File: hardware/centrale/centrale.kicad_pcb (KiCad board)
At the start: 2 copper layers, 70 x 110 mm, 57 parts, among them J1 MDCOG240128B6W, J2 Conn_BME280, J3 CONN_BME280_2, J4 RJ45, J5 Term_sel, Q1 BSS123, U1 MCP7940N-xSN, U2 TPS54228, U3 MCP2542FDxMF, Y1 32.768Khz

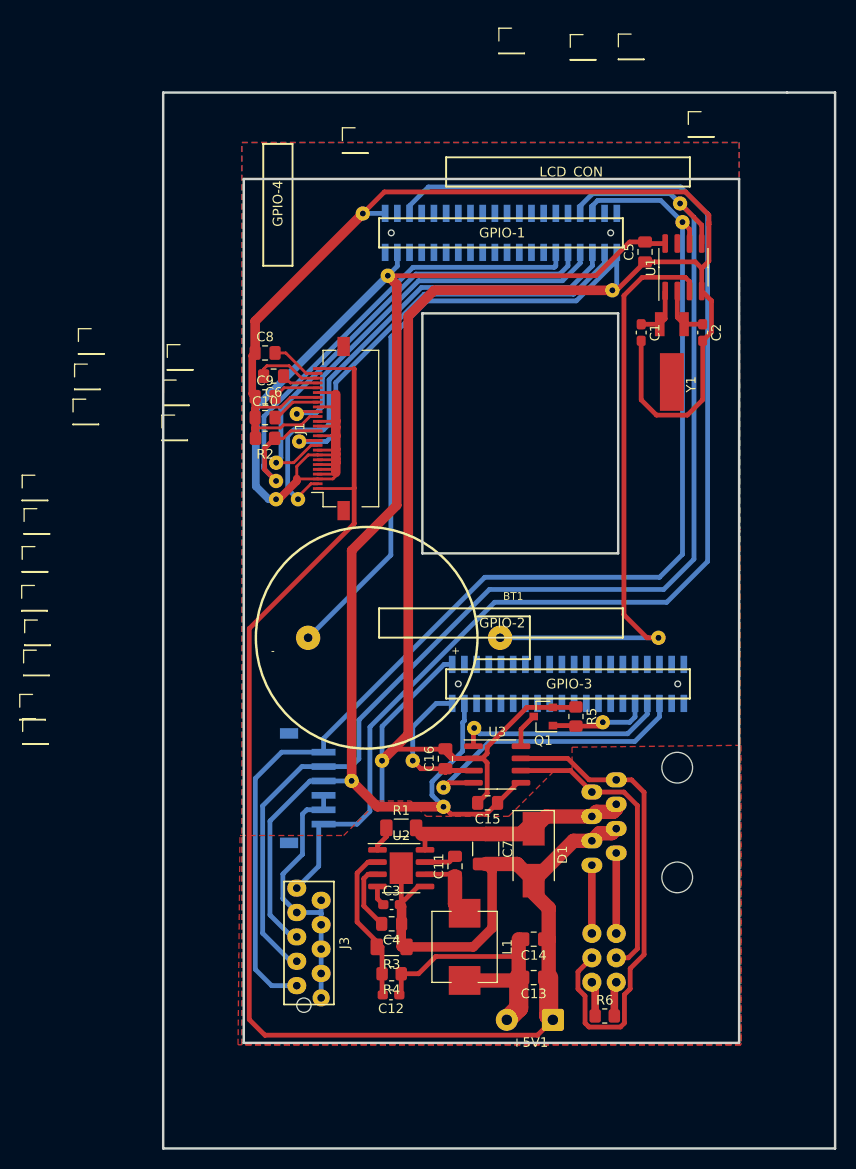
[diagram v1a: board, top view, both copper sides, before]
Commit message: Prepare for v2: fix display connector wiring, remplace the CAN transeiver with a pin-compatible one which is not out of stock, enlarge a bit the CPU cooling window.
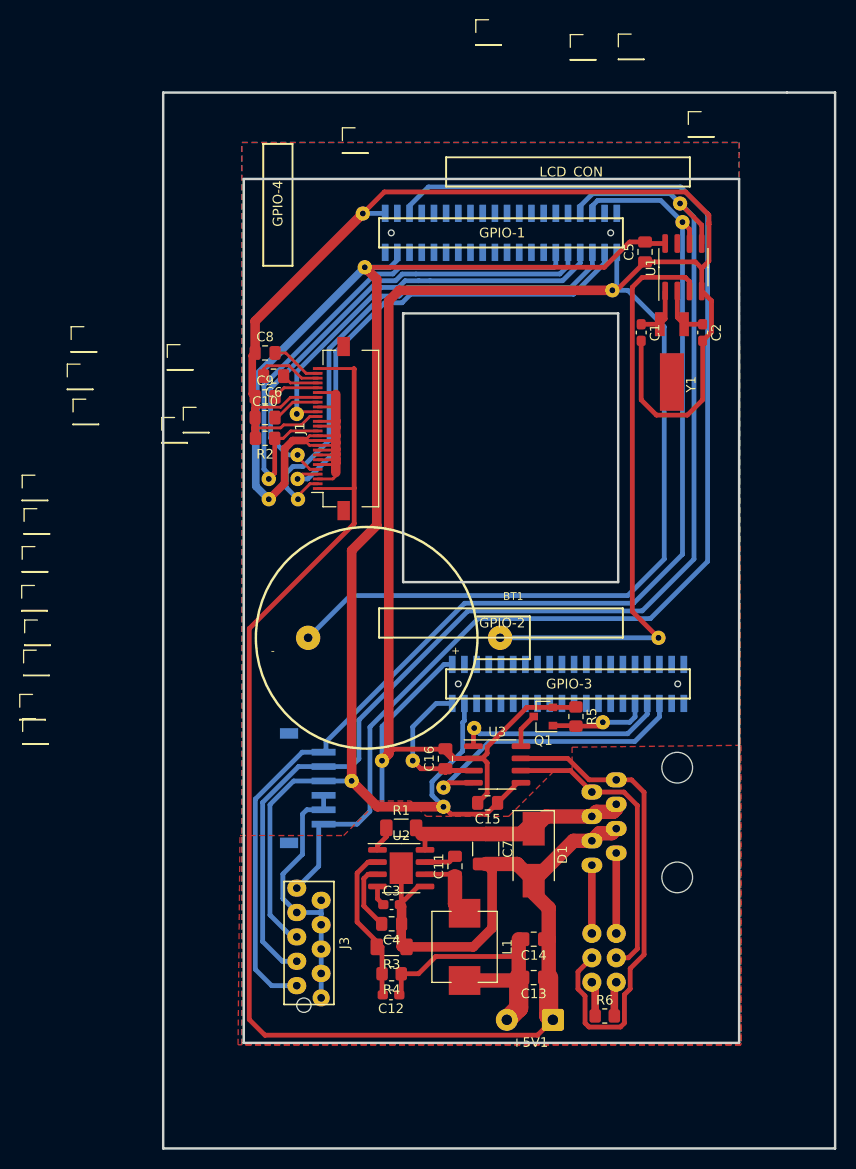
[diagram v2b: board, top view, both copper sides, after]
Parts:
- removed the REF** at (-42.5, -9.07)
- removed the REF** at (1.30, -40.4)
- added REF**: PinHeader_1x01_P2.54mm_Vertical, Connector_PinHeader_2.54mm:PinHeader_1x01_P2.54mm_Vertical, F.Cu at (-43.3, -9.28)
- added REF**: PinHeader_1x01_P2.54mm_Vertical, Connector_PinHeader_2.54mm:PinHeader_1x01_P2.54mm_Vertical, F.Cu at (-1.10, -41.3)
- U3: value MCP2542FDxMF -> TLE9250V
- moved REF** 3.90 mm to (-33.8, 0.18)
- moved REF** 2.37 mm to (-31.6, -0.88)
- moved REF** 0.76 mm to (-43.7, -5.38)
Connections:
- J1 pad 10: /D1-A0 -> +3V3
- J1 pad 11: /D0-SDA -> +3V3
- J1 pad 4: +3V3 -> /D0-SDA
- J1 pad 5: +3V3 -> /D1-A0
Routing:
- net GND: track 344.7 -> 355.9 mm
- net +3V3: track 216.1 -> 223.7 mm
- net /D0-SDA: track 45.6 -> 50.8 mm
- net /lime2/SCK: track 127.9 -> 126.3 mm
- net /V_BCKP: track 63.1 -> 61.7 mm
- net /SPI_CS: track 40.7 -> 42.0 mm
- net /SCL: track 52.9 -> 54.0 mm
- net /D1-A0: track 48.4 -> 49.2 mm
- net /lime2/SDA: track 130.9 -> 131.6 mm
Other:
- outline, holes or cut-outs redrawn

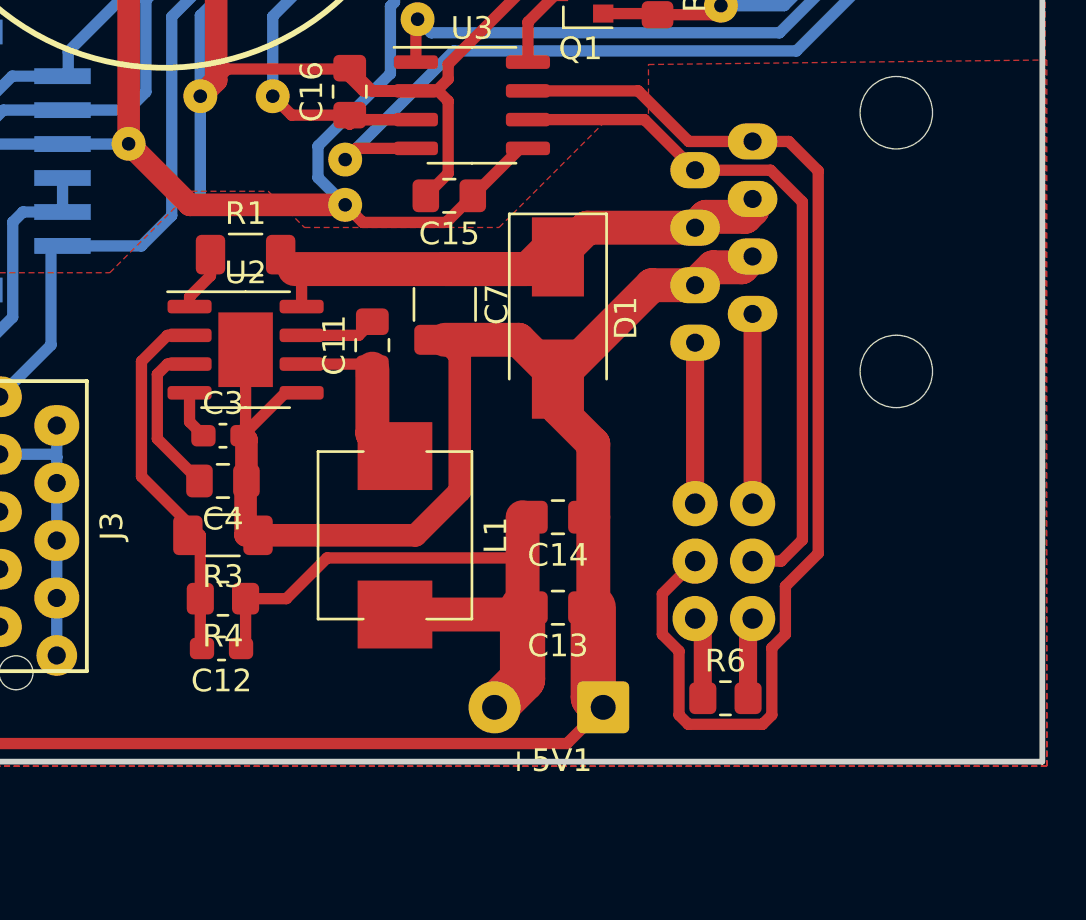
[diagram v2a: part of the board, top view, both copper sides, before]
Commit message: Use a MC24356 connector for the CPU power supply. Other minor cleanups
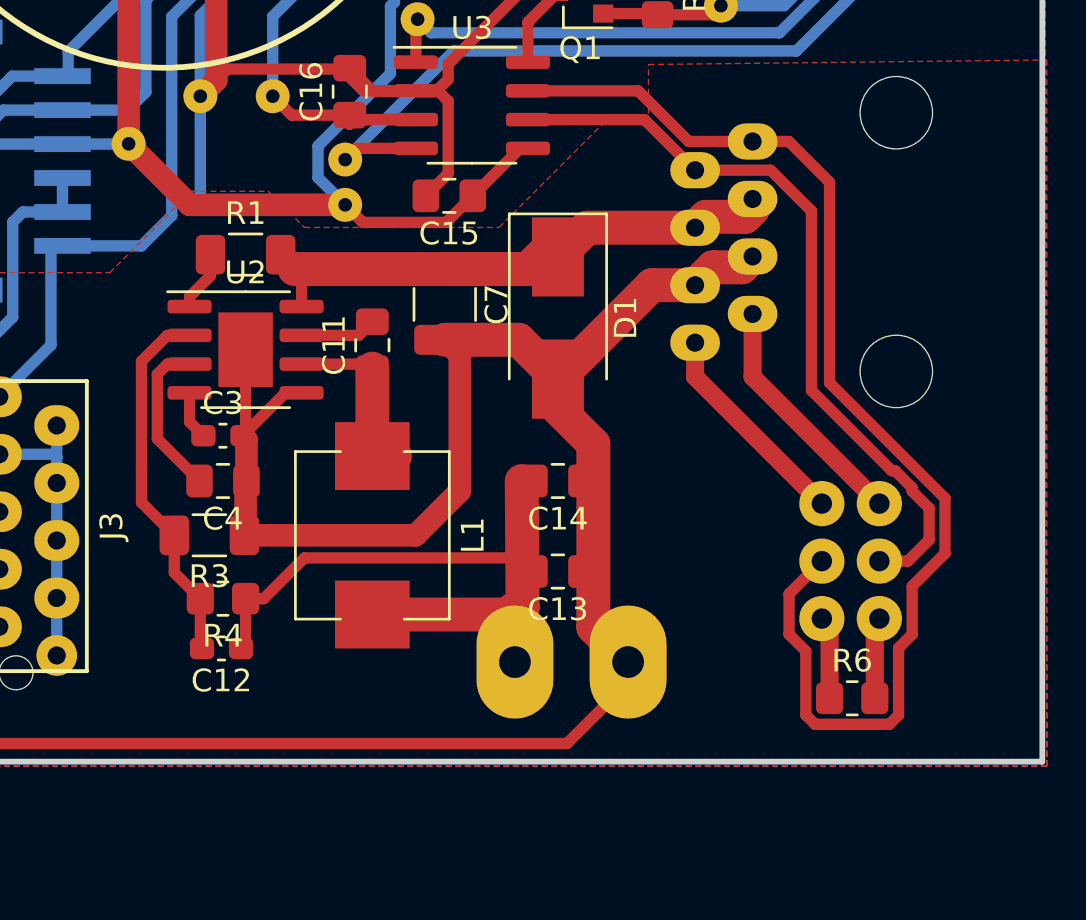
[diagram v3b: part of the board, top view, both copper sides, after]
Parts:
- +5V1: value CONN_01X02 -> 5V_LIME2; footprint Connector_Wire:SolderWire-0.5sqmm_1x02_P4.8mm_D0.9mm_OD2.3mm -> local:MC24356; moved to B.Cu
- moved J5 5.60 mm to (17.8, 52.6)
- moved R6 5.60 mm to (16.6, 61.2)
- moved +5V1 2.44 mm to (4.20, 59.6)
- moved C13 1.60 mm to (3.60, 55.6)
- moved C14 1.60 mm to (3.60, 51.6)
- moved L1 1.00 mm to (-4.60, 54.0)
- moved R3 0.60 mm to (-11.8, 54.0)
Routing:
- net Net-(J4-Pad2): track 31.1 -> 33.6 mm
- net Net-(J4-Pad8): track 7.11 -> 9.43 mm
- net Net-(J4-Pad7): track 8.38 -> 10.7 mm
- net Net-(J4-Pad1): track 51.3 -> 53.6 mm
- net GND2: track 174.6 -> 173.0 mm

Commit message: Change DC/DC output capacitors to 1210 size. Theses are better at 5V bias, hoping this will decrease the noise of the inductor.
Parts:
- C13, C14: footprint Capacitor_SMD:C_0805_2012Metric_Pad1.18x1.45mm_HandSolder -> Capacitor_SMD:C_1210_3225Metric_Pad1.33x2.70mm_HandSolder
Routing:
- net GND2: track 173.0 -> 166.8 mm

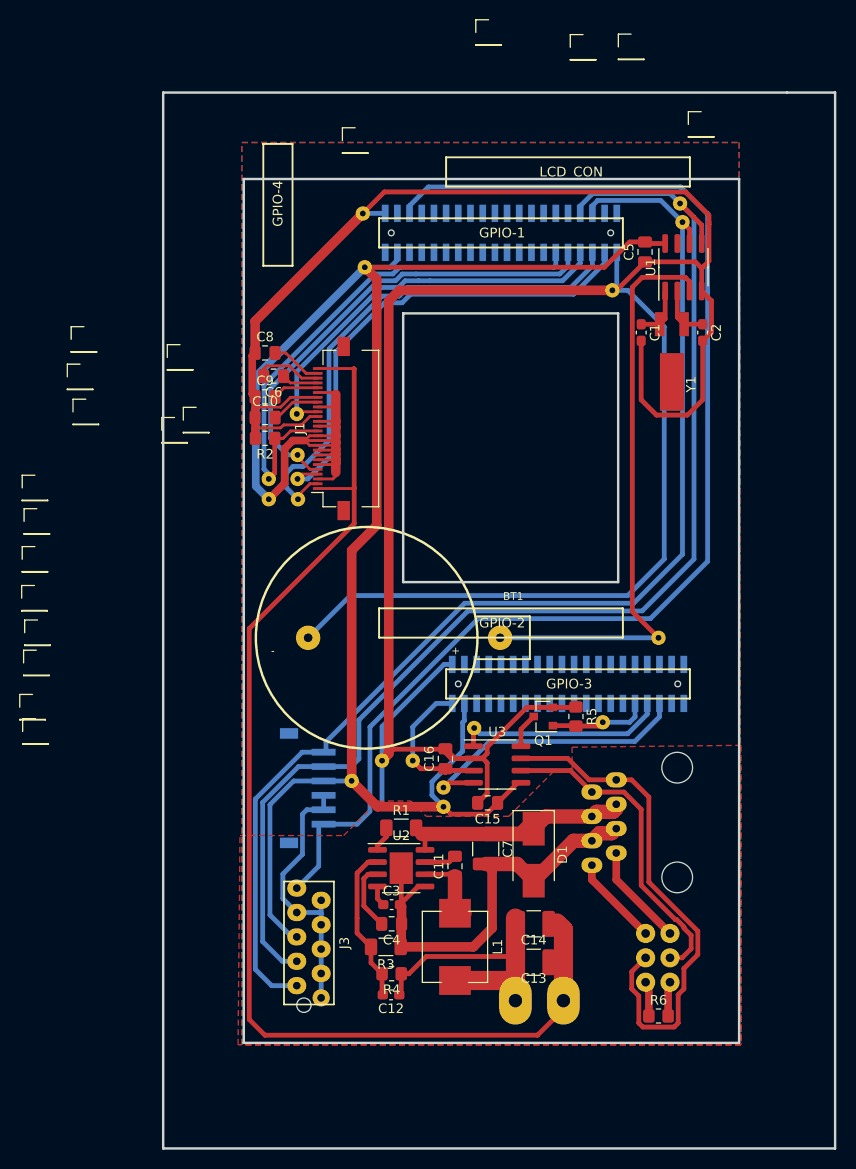
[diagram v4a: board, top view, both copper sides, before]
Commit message: More clearance
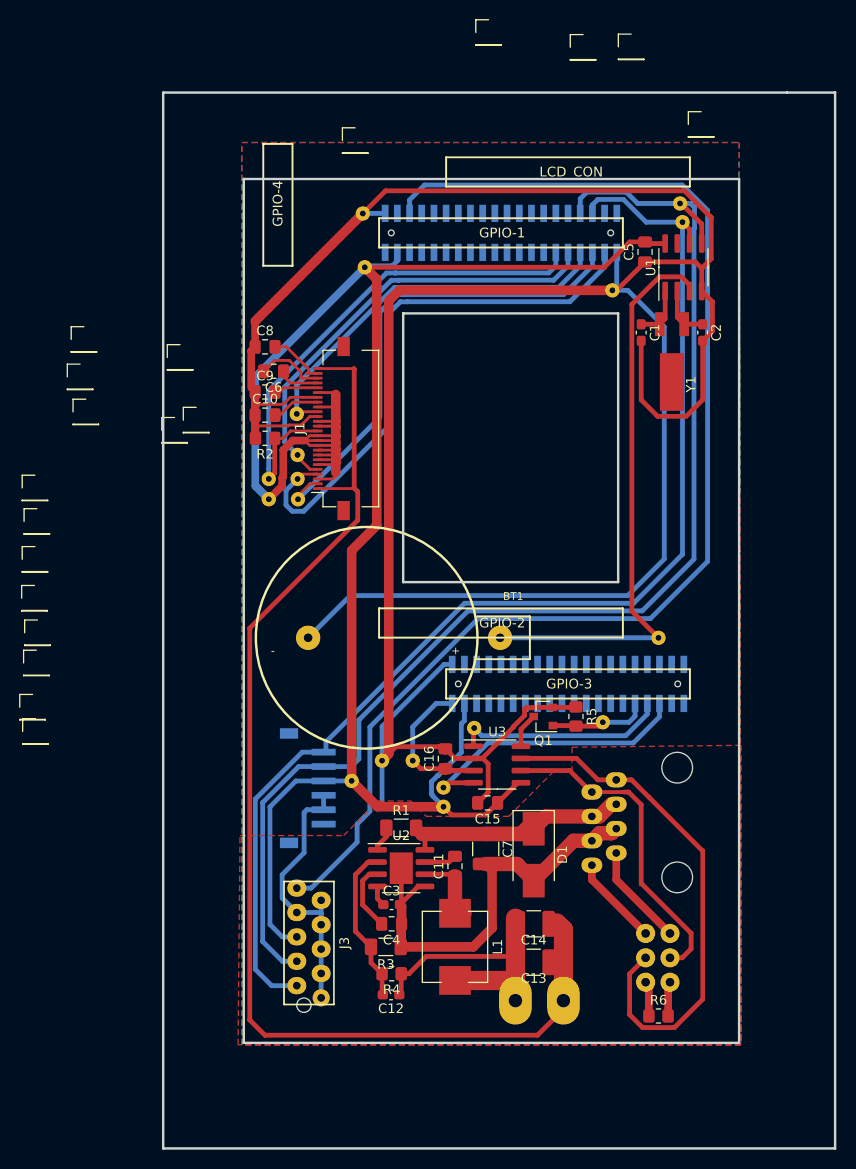
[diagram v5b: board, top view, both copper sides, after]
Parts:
- moved C8 0.64 mm to (-24.4, -8.51)
- moved C6 0.51 mm to (-23.5, -5.97)
- moved C9 0.51 mm to (-24.4, -3.81)
- moved C10 0.25 mm to (-24.4, -1.40)
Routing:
- net /D0-SDA: track 50.8 -> 57.9 mm
- net GND: track 355.9 -> 353.0 mm
- net /D1-A0: track 49.2 -> 46.6 mm
- net +3V3: track 223.7 -> 226.3 mm
- net /SCL: track 54.0 -> 51.5 mm
- net /XV0: track 7.05 -> 8.40 mm
- net /lime2/SDA: track 131.6 -> 132.9 mm
- net /V_BCKP: track 61.7 -> 60.6 mm
- net Net-(J4-Pad1): track 53.6 -> 54.4 mm
- net /VG: track 5.33 -> 6.05 mm
- net /lime2/LRADC0: track 134.6 -> 133.9 mm
- net /SPI_CS: track 42.0 -> 41.4 mm
- net /RSTB: track 56.7 -> 56.1 mm
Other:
- net class Default: clearance 0.2 -> 0.25
- rule trace_clearance: 0.2 -> 0.25

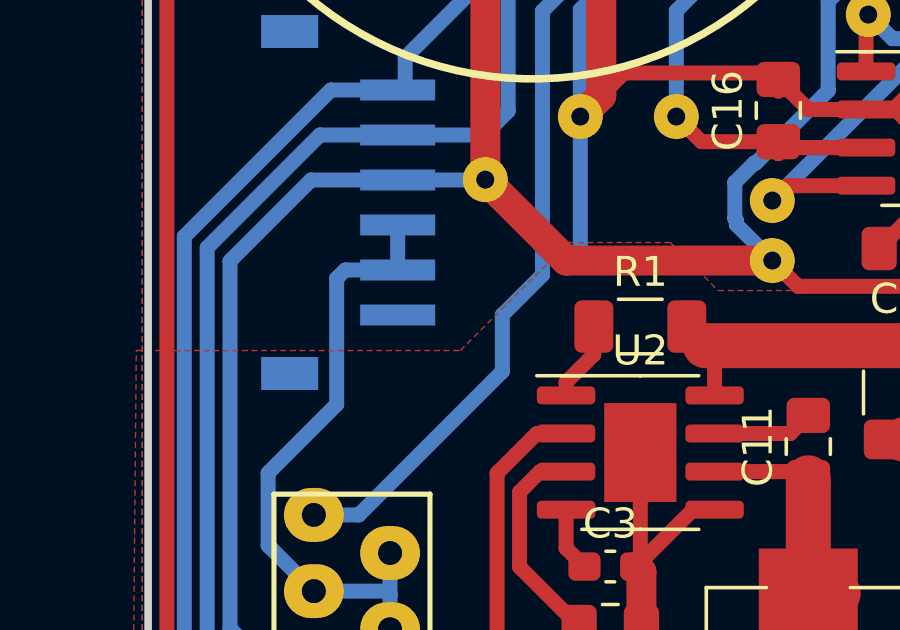
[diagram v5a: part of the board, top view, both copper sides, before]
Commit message: For next time: add a missing wire on LRADC
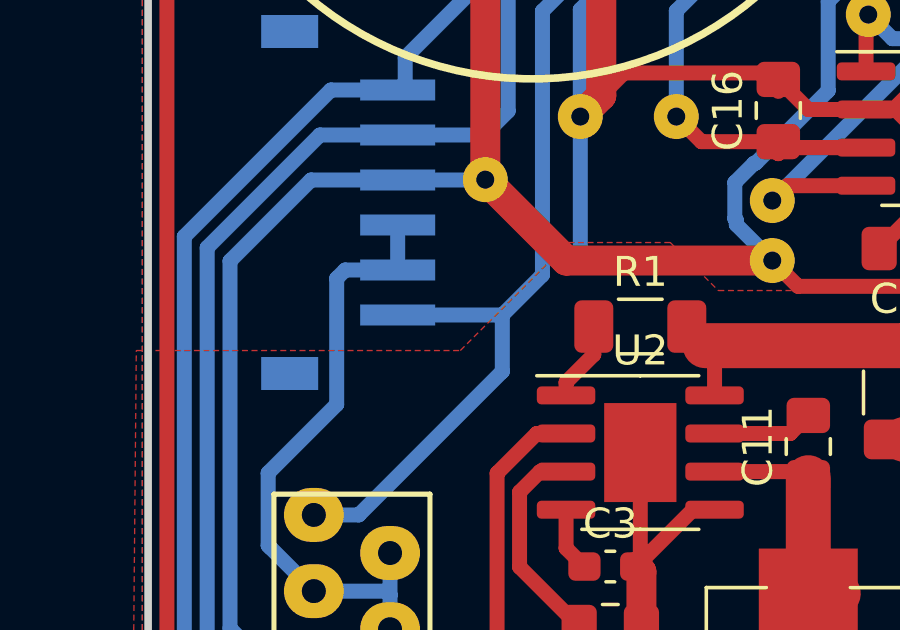
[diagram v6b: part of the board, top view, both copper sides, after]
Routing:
- net /lime2/LRADC0: track 133.9 -> 137.4 mm

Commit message: update capteur & centrale to new kicad format
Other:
- net class Default removed

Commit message: Name CANH and CANL nets
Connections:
- net /lime2/ECOL/LCD1_HSYNC/ATAIOR/KP_OUT6/SDC1_D2/CSI1_HSYNC/PH26 renamed /lime2/ECOL/LCD1_HSYNC/ATAIOR/KP_OUT6/SDC1_D2/CSI1_HSYNC/PH26
- net /lime2/ECRS/LCD1_DE/ATAIORDY/KP_OUT5/SDC1_D1/CSI1_FIELD/PH25 renamed /lime2/ECRS/LCD1_DE/ATAIORDY/KP_OUT5/SDC1_D1/CSI1_FIELD/PH25
- net /lime2/EMDIO/LCD1_D22/ATADACK/KP_OUT2/SDC1_CMD/CSI1_D22/PH22 renamed /lime2/EMDIO/LCD1_D22/ATADACK/KP_OUT2/SDC1_CMD/CSI1_D22/PH22
- net /lime2/ERXCK/LCD1_D18/ATAD14/KP_OUT0/SMC_SLK/EINT18/CSI1_D18/PH18 renamed /lime2/ERXCK/LCD1_D18/ATAD14/KP_OUT0/SMC_SLK/EINT18/CSI1_D18/PH18
- net /lime2/ERXD0/LCD1_D11/ATAD7/KP_IN3/MS_D3/EINT11/CSI1_D11/PH11 renamed /lime2/ERXD0/LCD1_D11/ATAD7/KP_IN3/MS_D3/EINT11/CSI1_D11/PH11
- net /lime2/ERXD1/LCD1_D10/ATAD6/KP_IN2/MS_D2/EINT10/CSI1_D10/PH10 renamed /lime2/ERXD1/LCD1_D10/ATAD6/KP_IN2/MS_D2/EINT10/CSI1_D10/PH10
- net /lime2/ERXD2/LCD1_D9/ATAD5/KP_IN1/MS_D1/EINT9/CSI1_D9/PH9 renamed /lime2/ERXD2/LCD1_D9/ATAD5/KP_IN1/MS_D1/EINT9/CSI1_D9/PH9
- net /lime2/ETEN/LCD1_D23/ATACS0/KP_OUT3/SDC1_CLK/CSI1_D23/PH23 renamed /lime2/ETEN/LCD1_D23/ATACS0/KP_OUT3/SDC1_CLK/CSI1_D23/PH23
- net /lime2/ETXCK/LCD1_CLK/ATACS1/KP_OUT4/SDC1_D0/CSI1_PCLK/PH24 renamed /lime2/ETXCK/LCD1_CLK/ATACS1/KP_OUT4/SDC1_D0/CSI1_PCLK/PH24
- net /lime2/ETXD0/LCD1_D17/ATAD13/KP_IN7/SMC_VCCEN/EINT17/CSI1_D17/PH17 renamed /lime2/ETXD0/LCD1_D17/ATAD13/KP_IN7/SMC_VCCEN/EINT17/CSI1_D17/PH17
- net /lime2/ETXD1/LCD1_D16/ATAD12/KP_IN6/SMC_DET/EINT16/CSI1_D16/PH16 renamed /lime2/ETXD1/LCD1_D16/ATAD12/KP_IN6/SMC_DET/EINT16/CSI1_D16/PH16
- net /lime2/ETXD2/LCD1_D15/ATAD11/KP_IN5/SMC_VPPPP/EINT15/CSI1_D15/PH15 renamed /lime2/ETXD2/LCD1_D15/ATAD11/KP_IN5/SMC_VPPPP/EINT15/CSI1_D15/PH15
- net /lime2/ETXD3/LCD1_D14/ATAD10/KP_IN4/SMC_VPPEN/EINT14/CSI1_D14/PH14 renamed /lime2/ETXD3/LCD1_D14/ATAD10/KP_IN4/SMC_VPPEN/EINT14/CSI1_D14/PH14
- net /lime2/ETXERR/LCD1_VSYNC/ATAIOW/KP_OUT7/SDC1_D3/CSI1_VSYNC/PH27 renamed /lime2/ETXERR/LCD1_VSYNC/ATAIOW/KP_OUT7/SDC1_D3/CSI1_VSYNC/PH27
- net /lime2/HPCOM/HPCOMFB renamed /lime2/HPCOM/HPCOMFB
- net /lime2/I2S_BCLK/AC97_BCLK/PB6 renamed /lime2/I2S_BCLK/AC97_BCLK/PB6
- net /lime2/I2S_DI/AC97_DI/SPDIF_DI/PB12 renamed /lime2/I2S_DI/AC97_DI/SPDIF_DI/PB12
- net /lime2/I2S_DO0/AC97_DO/PB8/SATA-PWR-EN renamed /lime2/I2S_DO0/AC97_DO/PB8/SATA-PWR-EN
- net /lime2/I2S_DO1/PB9 renamed /lime2/I2S_DO1/PB9
- net /lime2/I2S_DO2/PB10 renamed /lime2/I2S_DO2/PB10
- net /lime2/I2S_DO3/PB11 renamed /lime2/I2S_DO3/PB11
- net /lime2/I2S_LRCK/AC97_SYNC/PB7 renamed /lime2/I2S_LRCK/AC97_SYNC/PB7
- net /lime2/I2S_MCLK/AC97_MCLK/PB5 renamed /lime2/I2S_MCLK/AC97_MCLK/PB5
- net /lime2/IR0_RX/PB4 renamed /lime2/IR0_RX/PB4
- net /lime2/IR0_TX/SPDIF_MCLK/STANBYWFI/PB3 renamed /lime2/IR0_TX/SPDIF_MCLK/STANBYWFI/PB3
- net /lime2/JTAG_CK0/SPI2_CLK/PB15 renamed /lime2/JTAG_CK0/SPI2_CLK/PB15
- net /lime2/JTAG_DI0/SPI2_MISO/PB17 renamed /lime2/JTAG_DI0/SPI2_MISO/PB17
- net /lime2/JTAG_DO0/SPI2_MOSI/PB16 renamed /lime2/JTAG_DO0/SPI2_MOSI/PB16
- net /lime2/JTAG_MS0/SPI2_CS0/PB14 renamed /lime2/JTAG_MS0/SPI2_CS0/PB14
- net /lime2/LCD1_D0/ATAA0/UART3_TX/EINT0/CSI1_D0/PH0 renamed /lime2/LCD1_D0/ATAA0/UART3_TX/EINT0/CSI1_D0/PH0
- net /lime2/LCD1_D12/ATAD8/PS2_SCK1/EINT12/CSI1_D12/PH12 renamed /lime2/LCD1_D12/ATAD8/PS2_SCK1/EINT12/CSI1_D12/PH12
- net /lime2/LCD1_D13/ATAD9/PS2_SDA1/SMC_RST/EINT13/CSI1_D13/PH13 renamed /lime2/LCD1_D13/ATAD9/PS2_SDA1/SMC_RST/EINT13/CSI1_D13/PH13
- net /lime2/LCD1_D7/ATAD3/UART5_RX/MS_CLK/EINT7/CSI1_D7/PH7/I2S_DO1/PB9/USB0-DRV renamed /lime2/LCD1_D7/ATAD3/UART5_RX/MS_CLK/EINT7/CSI1_D7/PH7/I2S_DO1/PB9/USB0-DRV
- net /lime2/NDQS/PC24 renamed /lime2/NDQS/PC24
- net /lime2/SPI0_CS0/PC23 renamed /lime2/SPI0_CS0/PC23
- net /lime2/SPI2_CS1/SPDIF_DO/PB13 renamed /lime2/SPI2_CS1/SPDIF_DO/PB13
- net /lime2/TS1_CLK/CSI1_PCLK/SDC1_CMD/PG0 renamed /lime2/TS1_CLK/CSI1_PCLK/SDC1_CMD/PG0
- net /lime2/TS1_D0/CSI1_D0/SDC1_D2/CSI0_D8/PG4 renamed /lime2/TS1_D0/CSI1_D0/SDC1_D2/CSI0_D8/PG4
- net /lime2/TS1_D1/CSI1_D1/SDC1_D3/CSI0_D9/PG5 renamed /lime2/TS1_D1/CSI1_D1/SDC1_D3/CSI0_D9/PG5
- net /lime2/TS1_D2/CSI1_D2/UART3_TX/CSI0_D10/PG6 renamed /lime2/TS1_D2/CSI1_D2/UART3_TX/CSI0_D10/PG6
- net /lime2/TS1_D3/CSI1_D3/UART3_RX/CSI0_D11/PG7 renamed /lime2/TS1_D3/CSI1_D3/UART3_RX/CSI0_D11/PG7
- net /lime2/TS1_D4/CSI1_D4/UART3_RTS/CSI0_D12/PG8 renamed /lime2/TS1_D4/CSI1_D4/UART3_RTS/CSI0_D12/PG8
- net /lime2/TS1_D5/CSI1_D5/UART3_CTS/CSI0_D13/PG9 renamed /lime2/TS1_D5/CSI1_D5/UART3_CTS/CSI0_D13/PG9
- net /lime2/TS1_D6/CSI1_D6/UART4_TX/CSI0_D14/PG10 renamed /lime2/TS1_D6/CSI1_D6/UART4_TX/CSI0_D14/PG10
- net /lime2/TS1_D7/CSI1_D7/UART4_RX/CSI0_D15/PG11 renamed /lime2/TS1_D7/CSI1_D7/UART4_RX/CSI0_D15/PG11
- net /lime2/TS1_DVLD/CSI1_VSYNC/SDC1_D1/PG3 renamed /lime2/TS1_DVLD/CSI1_VSYNC/SDC1_D1/PG3
- net /lime2/TS1_ERR/CSI1_MLCK/SDC1_CLK/PG1 renamed /lime2/TS1_ERR/CSI1_MLCK/SDC1_CLK/PG1
- net /lime2/TS1_SYNC/CSI1_HSYNC/SDC1_D0/PG2 renamed /lime2/TS1_SYNC/CSI1_HSYNC/SDC1_D0/PG2
- net /lime2/TVOUT0/VGA-G renamed /lime2/TVOUT0/VGA-G
- net /lime2/TVOUT1/VGA-B renamed /lime2/TVOUT1/VGA-B
- net /lime2/TVOUT2/VGA-R renamed /lime2/TVOUT2/VGA-R
- net /lime2/TWI2_SCK/PB20 renamed /lime2/TWI2_SCK/PB20
- net /lime2/TWI2_SDA/PB21 renamed /lime2/TWI2_SDA/PB21
- net /lime2/UART0_RX/IR1_RX/PB23 renamed /lime2/UART0_RX/IR1_RX/PB23
- net /lime2/UART0_TX/IR1_TX/PB22 renamed /lime2/UART0_TX/IR1_TX/PB22
- net Net-(J4-Pad1) renamed /CANH
- net Net-(J4-Pad2) renamed /CANL
- C15 pad 1: +3V3 -> +3.3V
- C5 pad 2: +3V3 -> +3.3V
- GPIO-1 pad 3: +3V3 -> +3.3V
- GPIO-1 pad 34: /lime2/SDA -> /lime2/TWI1_SDA/PB19
- GPIO-1 pad 36: /lime2/SCK -> /lime2/TWI1_SCK/PB18
- GPIO-3 pad 3: +3V3 -> +3.3V
- GPIO-3 pad 31: /lime2/CAN_EN -> /lime2/ERXERR/LCD1_D19/ATAD15/KP_OUT1/SMC_SDA/EINT19/CSI1_D19/PH19
- GPIO-3 pad 33: /lime2/CAN_TX -> /lime2/ERXDV/LCD1_D20/ATAOE/CAN_TX/EINT20/CSI1_D20/PH20
- GPIO-3 pad 35: /lime2/CAN_RX -> /lime2/EMDC/LCD1_D21/ATADREQ/CAN_RX/EINT21/CSI1_D21/PH21
- J1 pad 10: +3V3 -> +3.3V
- J1 pad 11: +3V3 -> +3.3V
- J1 pad 12: +3V3 -> +3.3V
- J1 pad 14: +3V3 -> +3.3V
- J1 pad 15: +3V3 -> +3.3V
- J1 pad 18: +3V3 -> +3.3V
- J1 pad 21: +3V3 -> +3.3V
- J1 pad 3: +3V3 -> +3.3V
- J1 pad 6: +3V3 -> +3.3V
- J1 pad 7: +3V3 -> +3.3V
- J1 pad 8: +3V3 -> +3.3V
- J1 pad 9: +3V3 -> +3.3V
- J2 pad 4: +3V3 -> +3.3V
- J2 pad 5: /lime2/SDA -> /lime2/TWI1_SDA/PB19
- J2 pad 6: /lime2/SCK -> /lime2/TWI1_SCK/PB18
- J3 pad 2: /lime2/SCK -> /lime2/TWI1_SCK/PB18
- J3 pad 4: /lime2/SDA -> /lime2/TWI1_SDA/PB19
- J3 pad 6: +3V3 -> +3.3V
- Q1 pad 1: /lime2/CAN_EN -> /lime2/ERXERR/LCD1_D19/ATAD15/KP_OUT1/SMC_SDA/EINT19/CSI1_D19/PH19
- R5 pad 2: /lime2/CAN_EN -> /lime2/ERXERR/LCD1_D19/ATAD15/KP_OUT1/SMC_SDA/EINT19/CSI1_D19/PH19
- U1 pad 5: /lime2/SDA -> /lime2/TWI1_SDA/PB19
- U1 pad 6: /lime2/SCK -> /lime2/TWI1_SCK/PB18
- U1 pad 7: Net-(U1-Pad7) -> unconnected-(U1-Pad7)
- U1 pad 8: +3V3 -> +3.3V
- U3 pad 1: /lime2/CAN_TX -> /lime2/ERXDV/LCD1_D20/ATAOE/CAN_TX/EINT20/CSI1_D20/PH20
- U3 pad 4: /lime2/CAN_RX -> /lime2/EMDC/LCD1_D21/ATADREQ/CAN_RX/EINT21/CSI1_D21/PH21
- U3 pad 5: +3V3 -> +3.3V
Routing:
- net +3V3: track 226.3 -> 0.00 mm
- net +3.3V: track 0.00 -> 226.3 mm
- net /lime2/TWI1_SDA/PB19: track 0.00 -> 132.9 mm
- net /lime2/SDA: track 132.9 -> 0.00 mm
- net /lime2/TWI1_SCK/PB18: track 0.00 -> 126.4 mm
- net /lime2/SCK: track 126.4 -> 0.00 mm
- net /lime2/EMDC/LCD1_D21/ATADREQ/CAN_RX/EINT21/CSI1_D21/PH21: track 0.00 -> 30.3 mm
- net /lime2/CAN_RX: track 30.3 -> 0.00 mm
- net /lime2/ERXDV/LCD1_D20/ATAOE/CAN_TX/EINT20/CSI1_D20/PH20: track 0.00 -> 22.3 mm
- net /lime2/CAN_TX: track 22.3 -> 0.00 mm
- net /lime2/ERXERR/LCD1_D19/ATAD15/KP_OUT1/SMC_SDA/EINT19/CSI1_D19/PH19: track 0.00 -> 10.3 mm
- net /lime2/CAN_EN: track 10.3 -> 0.00 mm
